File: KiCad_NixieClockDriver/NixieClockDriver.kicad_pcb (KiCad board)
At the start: 2 copper layers, 115.6 x 33 mm, 70 parts, among them J1 Multiplexer, J2 sterowanie_lamp, J3 BOOT_0, J4 HV_OUT, J5 Barrel_Jack, J6 SWD, Q1 MPSA42, Q10 MPSA42, Q11 BC557, Q12 IRF740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

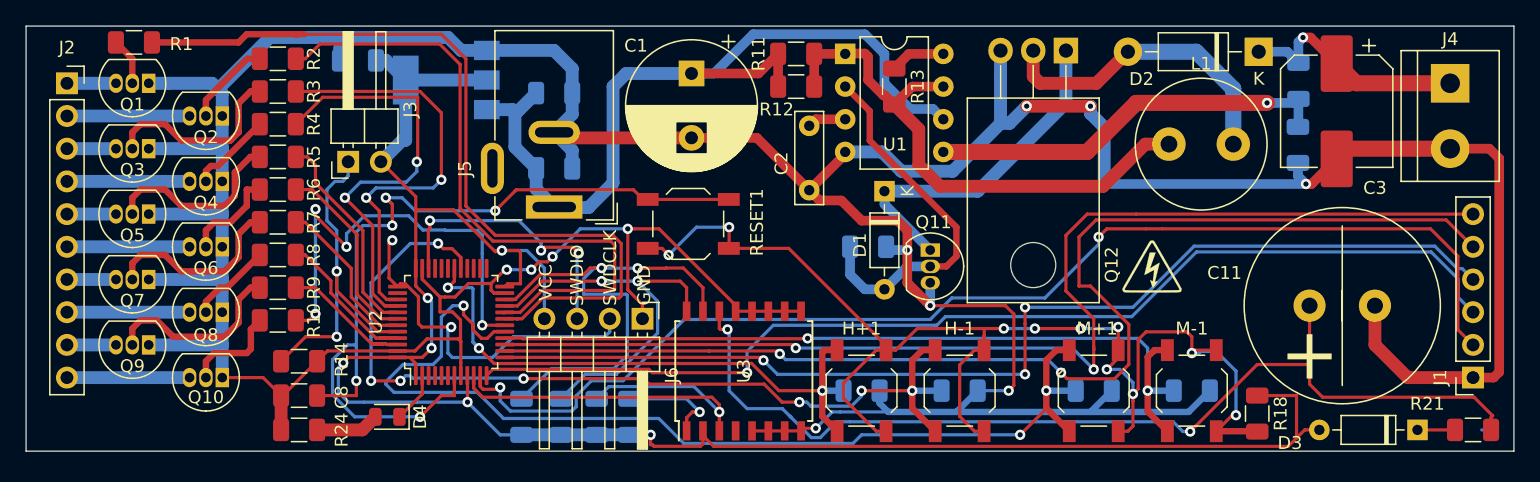
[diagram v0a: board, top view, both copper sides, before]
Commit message: Fixed reversed transistor in driver schematic
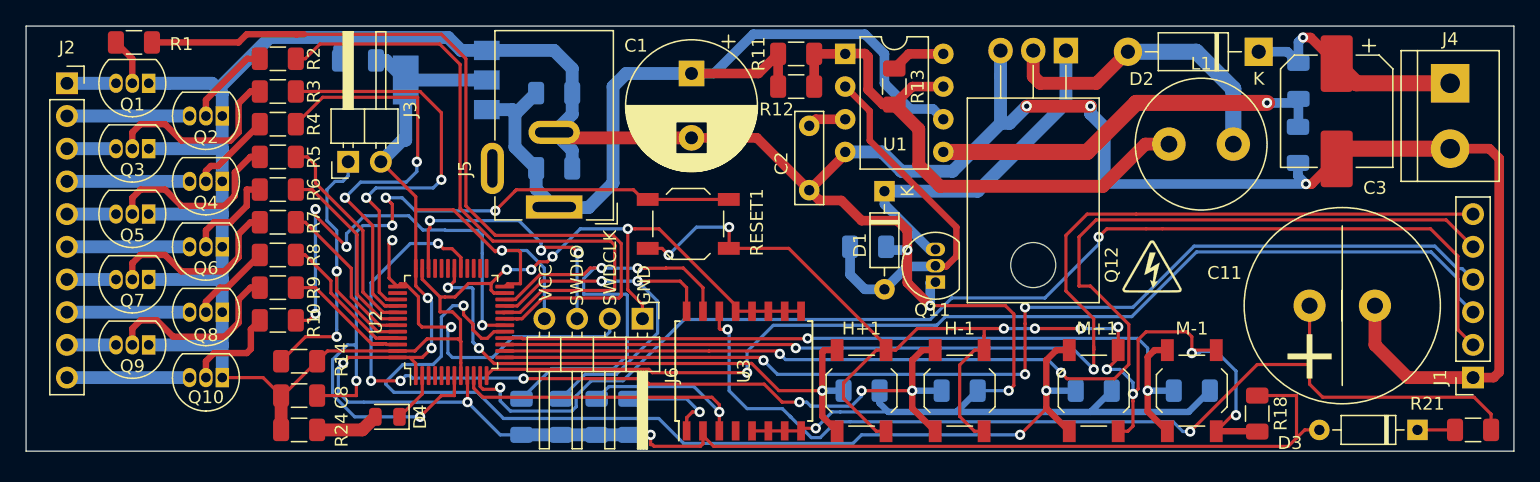
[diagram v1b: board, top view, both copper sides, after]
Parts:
- moved Q11 2.52 mm to (118.3, 155.1), turned to 90 degrees
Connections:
- Q11 pad 1: Net-(D1-Pad1) -> GND
- Q11 pad 3: GND -> Net-(D1-Pad1)
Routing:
- net /VBAT: track 79.8 -> 78.9 mm
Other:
- board text removed: "WOJCIECH KLIMEK - PROJEKT PTM 2 2019"
